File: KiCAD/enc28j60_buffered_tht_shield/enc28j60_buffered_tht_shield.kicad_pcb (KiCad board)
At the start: 2 copper layers, 68.6 x 53.3 mm, 38 parts, among them J1 AVR-ISP-6, J2 RJ45_MagJack_LMJTAB881X43M-L, J3 Conn_01x03_Male, P1 CONN_01X01, P2 CONN_01X01, P3 CONN_01X01, P4 CONN_01X01, P5 Digital, P6 Power, P7 Digital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

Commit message: v1
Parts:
- moved U3 0.09 mm to (163.2, 85.7)
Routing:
- net GND: track 24.6 -> 51.1 mm, vias 10 -> 12

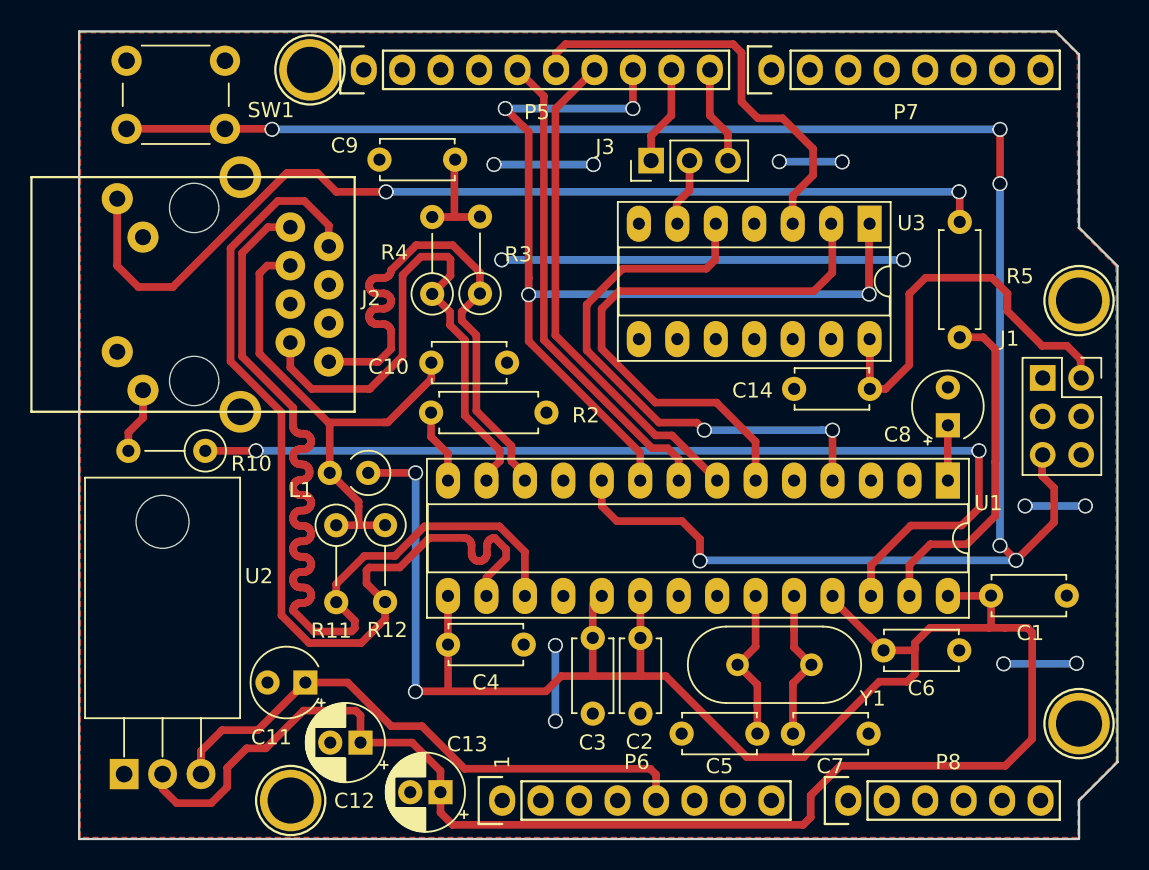
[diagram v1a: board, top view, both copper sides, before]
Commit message: Added AT24MAC402-602 as an option.
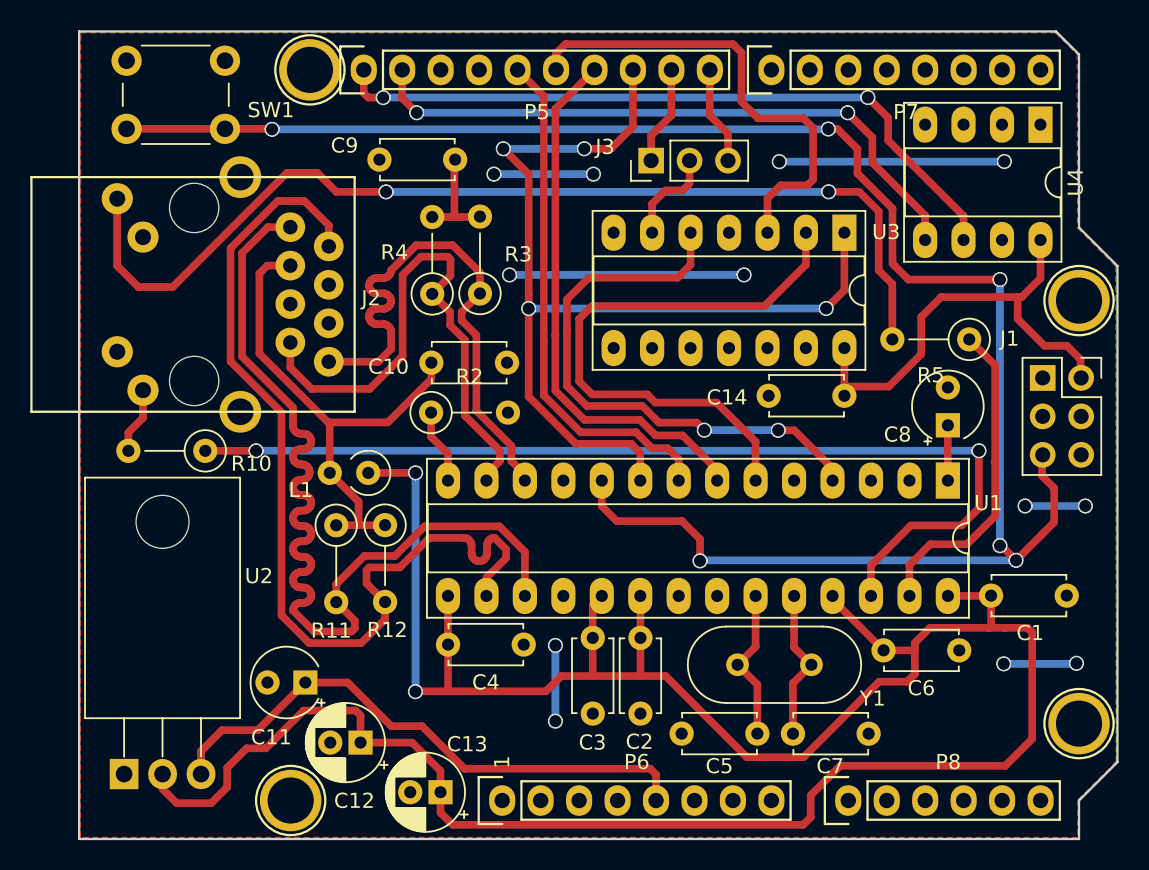
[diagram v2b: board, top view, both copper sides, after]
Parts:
- added U4: AT24MAC402-SSHM, Package_DIP:DIP-8_W7.62mm_Socket_LongPads, F.Cu at (174.5, 79.2)
- R2, R5: footprint Resistor_THT:R_Axial_DIN0207_L6.3mm_D2.5mm_P7.62mm_Horizontal -> Resistor_THT:R_Axial_DIN0207_L6.3mm_D2.5mm_P5.08mm_Vertical
- moved U3 1.77 mm to (161.5, 86.3)
- moved C14 1.74 mm to (161.5, 97.1)
- moved R5 0.64 mm to (169.8, 93.4), turned to 180 degrees
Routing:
- net /A5(SCL): track 0.00 -> 47.0 mm, vias 0 -> 2
- net /A4(SDA): track 0.00 -> 42.2 mm, vias 0 -> 2
- net +5V: track 64.8 -> 68.6 mm
- net /12(MISO): track 28.6 -> 31.7 mm
- net /Reset: track 126.4 -> 123.8 mm
- net /11(**/MOSI): track 33.3 -> 35.8 mm
- net /13(SCK): track 32.1 -> 34.3 mm
- net Net-(J2-Pad9): track 66.3 -> 68.3 mm
- net /INT_PIN: track 4.60 -> 6.45 mm
- net /LEDA: track 22.7 -> 21.4 mm
- net /MISO_ENC: track 37.4 -> 38.6 mm
- net /INT_ENC: track 36.8 -> 37.6 mm

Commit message: Final ( ? ) v2
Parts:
- added ?: , Aesthetics:OSHW-LOGO-M, F.Cu at (170.4, 118.5)
- added C15: 100 nF, Capacitor_THT:C_Disc_D4.7mm_W2.5mm_P5.00mm, F.Cu at (173.3, 90.7)
- J3: value Conn_01x03_Male -> Conn_01x05_Male; footprint Connector_PinHeader_2.54mm:PinHeader_1x03_P2.54mm_Vertical -> Connector_PinHeader_2.54mm:PinHeader_1x05_P2.54mm_Vertical
- moved J3 3.32 mm to (145.5, 81.5)
- moved C1 0.68 mm to (171.9, 110.3), turned to 270 degrees
- moved R5 0.53 mm to (169.4, 93.7)
- moved U4 0.24 mm to (174.5, 78.9)
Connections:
- J3 pad 1: /9(**) -> /10(**/SS)
- J3 pad 2: /INT_PIN -> /SS_PIN
- J3 pad 3: /8 -> /9(**)
- U1 pad 9: /10(**/SS) -> /SS_PIN
- U3 pad 1: /10(**/SS) -> /SS_PIN
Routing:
- net /SS_PIN: track 0.00 -> 65.9 mm, vias 0 -> 4
- net /10(**/SS): track 65.9 -> 6.83 mm, vias 4 -> 0
- net GND: track 50.8 -> 23.6 mm, vias 12 -> 8
- net +5V: track 68.6 -> 75.4 mm
- net /12(MISO): track 31.7 -> 28.2 mm
- net /11(**/MOSI): track 35.8 -> 38.0 mm
- net /INT_PIN: track 6.45 -> 8.35 mm
- net /MISO_ENC: track 38.6 -> 40.2 mm, vias 0 -> 2
- net /A5(SCL): track 47.0 -> 48.4 mm
- net Net-(J2-Pad9): track 68.3 -> 69.6 mm
- net /A4(SDA): track 42.2 -> 43.3 mm
- net /8: track 6.49 -> 7.20 mm
- net +3V3: track 173.8 -> 174.5 mm
- net /INT_ENC: track 37.6 -> 38.1 mm, vias 2 -> 4
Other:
- board text added: "DCI 2020"
- board text added: "ENC Ether v2"
- board text added: "www.nephelae.eu"

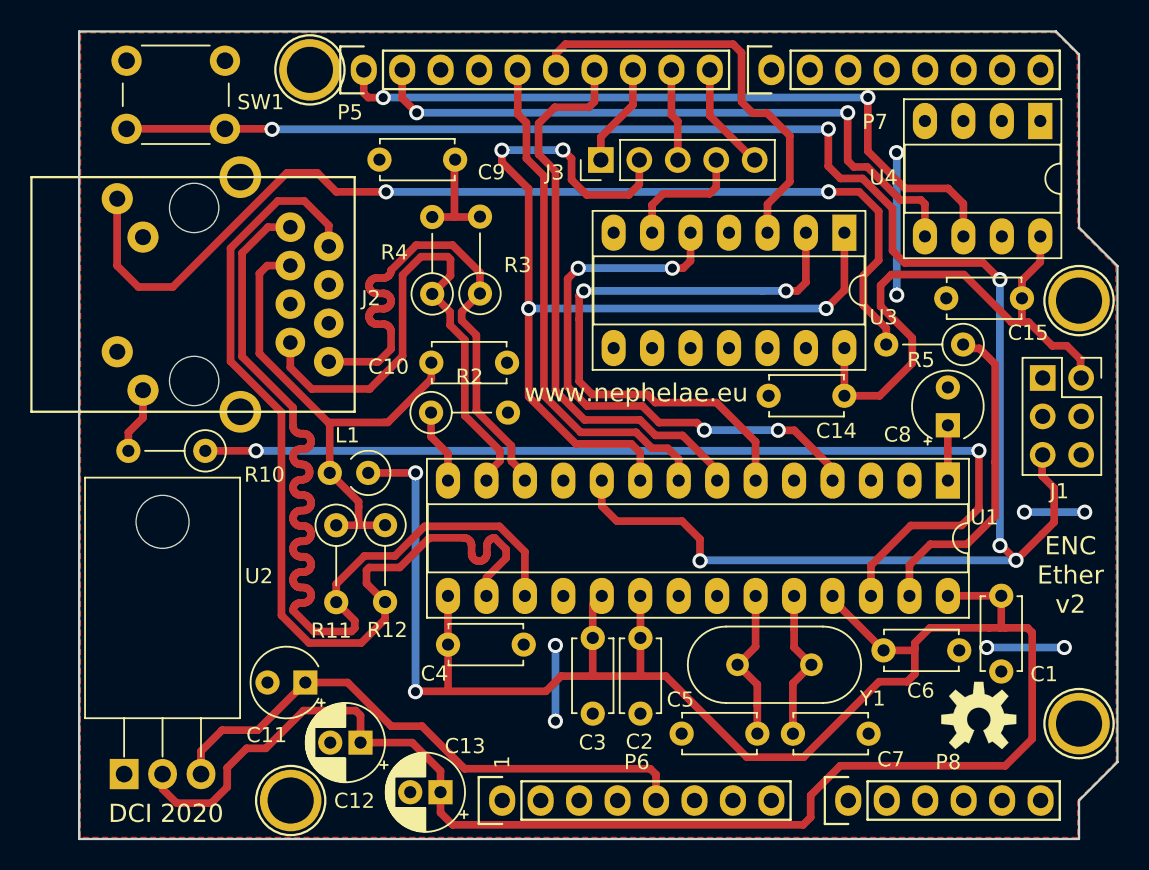
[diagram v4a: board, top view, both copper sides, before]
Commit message: Some changes to ground plane.
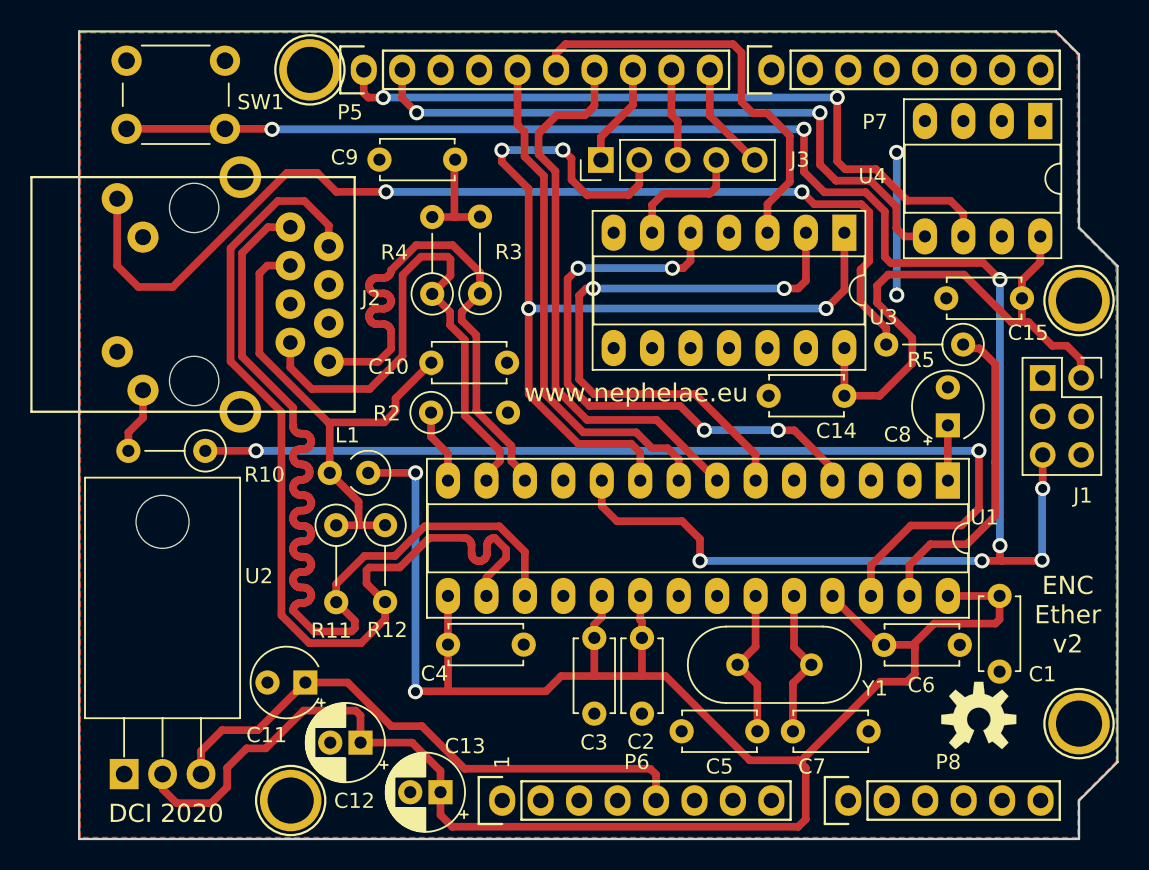
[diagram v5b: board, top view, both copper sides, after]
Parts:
- moved C6 0.37 mm to (169.2, 113.5)
- moved C7 0.15 mm to (158.1, 119.3)
- moved C5 0.15 mm to (155.8, 119.3)
- moved C1 0.11 mm to (171.8, 110.3)
- moved C2 0.10 mm to (148.2, 118.1)
- moved C3 0.10 mm to (145.0, 118.1)
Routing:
- net +3V3: track 174.5 -> 150.6 mm
- net GND: track 23.6 -> 9.49 mm, vias 8 -> 2
- net Net-(J2-Pad9): track 69.6 -> 68.8 mm
- net /11(**/MOSI): track 38.0 -> 37.3 mm
- net /MISO_ENC: track 40.2 -> 39.5 mm
- net /Reset: track 123.7 -> 124.1 mm, vias 6 -> 8

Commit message: Fix ethernet differential pair length, skew. Fix LMJTAB881X43M Ground Pin. Added jumper for I2C address selection.
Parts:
- removed ?: , Aesthetics:OSHW-LOGO-M
- added J4: Conn_01x03_Male, Connector_PinHeader_2.54mm:PinHeader_1x03_P2.54mm_Vertical, F.Cu at (157.7, 79.2)
- R2: footprint Resistor_THT:R_Axial_DIN0207_L6.3mm_D2.5mm_P5.08mm_Vertical -> Resistor_THT:R_Axial_DIN0207_L6.3mm_D2.5mm_P2.54mm_Vertical
- moved C10 18.0 mm to (123.0, 102.6), turned to 0 degrees
- moved L1 13.7 mm to (132.6, 115.6), turned to 90 degrees
- moved C9 11.9 mm to (142.2, 85.1), turned to 225 degrees
- moved R3 6.42 mm to (138.9, 96.6)
- moved R4 6.40 mm to (135.7, 96.6)
- moved J3 4.85 mm to (140.6, 81.5)
- moved R2 2.11 mm to (132.7, 96.7), turned to 270 degrees
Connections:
- C14 pad 1: +5V -> VCC
- C15 pad 1: +5V -> VCC
- J1 pad 1: /12(MISO) -> (no net)
- J1 pad 2: +5V -> VCC
- J1 pad 3: /13(SCK) -> (no net)
- J1 pad 4: /11(**/MOSI) -> (no net)
- P6 pad 3: /Reset -> (no net)
- P6 pad 4: +3V3 -> (no net)
- P8 pad 5: /A4(SDA) -> (no net)
- P8 pad 6: /A5(SCL) -> (no net)
- U3 pad 14: +5V -> VCC
- U4 pad 1: GND -> /A_A0
- U4 pad 7: GND -> (no net)
- U4 pad 8: +5V -> VCC
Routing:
- net VCC: track 0.00 -> 59.8 mm
- net +5V: track 75.7 -> 37.7 mm
- net /TPIN-: track 37.4 -> 63.0 mm
- net /TPIN+: track 37.0 -> 61.2 mm
- net /A_A0: track 0.00 -> 18.5 mm
- net GND: track 9.49 -> 27.7 mm, vias 2 -> 8
- net +3V3: track 150.6 -> 135.8 mm, vias 2 -> 0
- net /11(**/MOSI): track 37.3 -> 44.7 mm
- net /13(SCK): track 34.2 -> 38.7 mm
- net /10(**/SS): track 6.83 -> 11.1 mm
- net Net-(C10-Pad2): track 34.4 -> 38.3 mm, vias 0 -> 2
- net /INT_PIN: track 8.35 -> 5.08 mm
- net /9(**): track 6.13 -> 8.50 mm
- net Net-(R2-Pad1): track 4.95 -> 7.04 mm
- net Net-(J2-Pad9): track 68.8 -> 70.7 mm
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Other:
- board text added: "ENC Ether v3"
- board text removed: "ENC Ether v2"
